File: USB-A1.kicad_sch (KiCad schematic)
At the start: 23 parts, among them J10 USB3_A, J9 USB3_A, U18 UCS2114-1-V/G4, U19 TPD4E02B04DQA, U20 TPD4E02B04DQA, U32 TPD4E02B04DQA

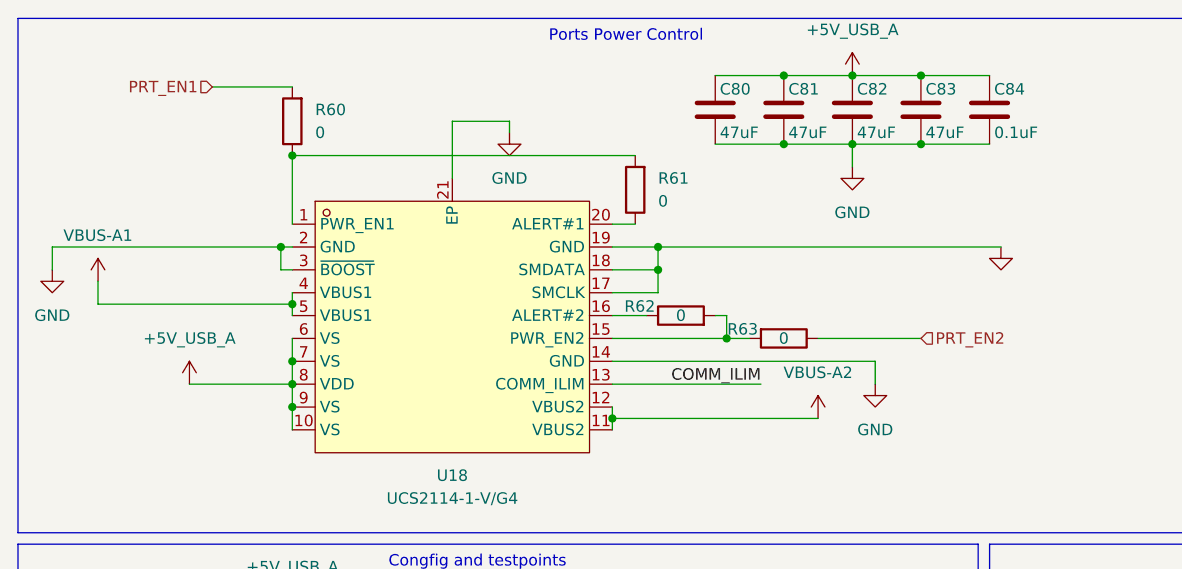
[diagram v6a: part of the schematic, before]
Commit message: minor schematic fixes, footprints changes, layout improvements
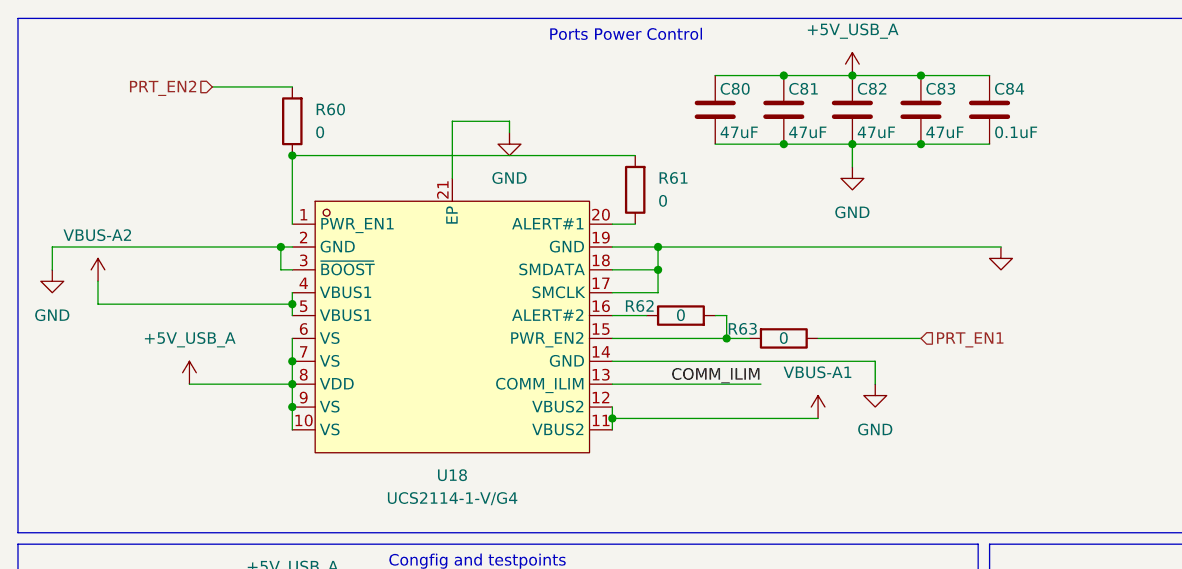
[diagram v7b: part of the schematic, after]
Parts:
- TP5, TP6: footprint TestPoint:TestPoint_Loop_D1.80mm_Drill1.0mm_Beaded -> TestPoint:TestPoint_Pad_D1.0mm
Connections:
- net PRT_EN1: now also R63.1; no longer R60.2
- net PRT_EN2: now also R60.2; no longer R63.1
- net VBUS-A1: now also U18.11 (VBUS2), U18.12 (VBUS2); no longer U18.4 (VBUS1), U18.5 (VBUS1)
- net VBUS-A2: now also U18.4 (VBUS1), U18.5 (VBUS1); no longer U18.11 (VBUS2), U18.12 (VBUS2)
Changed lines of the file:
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@@
 	(hierarchical_label "PRT_EN2"
+		(shape input)
+		(at 36.83 20.32 180)
+		(effects
+			(font
+				(size 1.27 1.27)
+			)
+			(justify right)
+		)
+	)
+	(hierarchical_label "PRT_EN1"
 		(shape input)
 		(at 115.57 48.26 0)
@@
 		)
 	)
-	(hierarchical_label "PRT_EN1"
-		(shape input)
-		(at 36.83 20.32 180)
-		(effects
-			(font
-				(size 1.27 1.27)
-			)
-			(justify right)
-		)
-	)
 	(rule_area
 		(polyline
@@
 	(symbol
 		(lib_id "power:VBUS")
+		(at 104.14 57.15 0)
+		(unit 1)
+		(exclude_from_sim no)
+		(in_bom yes)
+		(on_board yes)
+		(dnp no)
+		(fields_autoplaced yes)
+		(property "Reference" "#PWR0140"
+			(at 104.14 60.96 0)
+			(effects
+				(font
+					(size 1.27 1.27)
+				)
+				(hide yes)
+			)
+		)
+		(property "Value" "VBUS-A1"
+			(at 104.14 52.07 0)
+			(effects
+				(font
+					(size 1.27 1.27)
+				)
+			)
+		)
+		(property "Footprint" ""
+			(at 104.14 57.15 0)
+			(effects
+				(font
+					(size 1.27 1.27)
+				)
+				(hide yes)
+			)
+		)
+		(property "Datasheet" ""
+			(at 104.14 57.15 0)
+			(effects
+				(font
+					(size 1.27 1.27)
+				)
+				(hide yes)
+			)
+		)
+		(property "Description" "Power symbol creates a global label with name \"VBUS\""
+			(at 104.14 57.15 0)
+			(effects
+				(font
+					(size 1.27 1.27)
+				)
+				(hide yes)
+			)
+		)
+		(pin "1"
+		)
+		(instances
+			(project "USB_hub"
+				(path "/a2586c28-95f1-49e6-9254-37d7a8473e53/10c83c9e-05bd-4fa1-b7e1-a721413825c3"
+					(reference "#PWR0140")
+					(unit 1)
+				)
+			)
+		)
+	)
+	(symbol
+		(lib_id "Device:LED")
+		(at 189.23 93.98 180)
+		(unit 1)
+		(exclude_from_sim no)
+		(in_bom yes)
+		(on_board yes)
+		(dnp no)
+		(fields_autoplaced yes)
+		(property "Reference" "D7"
+			(at 190.8175 86.36 0)
+			(effects
+				(font
+					(size 1.27 1.27)
+				)
+			)
+		)
+		(property "Value" "GREEN"
+			(at 190.8175 88.9 0)
+			(effects
+				(font
+					(size 1.27 1.27)
+				)
+			)
+		)
+		(property "Footprint" "LED_SMD:LED_0603_1608Metric"
+			(at 189.23 93.98 0)
+			(effects
+				(font
+					(size 1.27 1.27)
+				)
+				(hide yes)
+			)
+		)
+		(property "Datasheet" "~"
+			(at 189.23 93.98 0)
+			(effects
+				(font
+					(size 1.27 1.27)
+				)
+				(hide yes)
+			)
+		)
+		(property "Description" "Light emitting diode"
+			(at 189.23 93.98 0)
+			(effects
+				(font
+					(size 1.27 1.27)
+				)
+				(hide yes)
+			)
+		)
+		(property "Sim.Pins" "1=K 2=A"
+			(at 189.23 93.98 0)
+			(effects
+				(font
+					(size 1.27 1.27)
+				)
+				(hide yes)
+			)
+		)
+		(property "LCSC Part" "C22371298"
+			(at 189.23 93.98 0)
+			(effects
+				(font
+					(size 1.27 1.27)
+				)
+				(hide yes)
+			)
+		)
+		(pin "1"
+		)
+		(pin "2"
+		)
+		(instances
+			(project "USB_hub"
+				(path "/a2586c28-95f1-49e6-9254-37d7a8473e53/10c83c9e-05bd-4fa1-b7e1-a721413825c3"
+					(reference "D7")
+					(unit 1)
+				)
+			)
+		)
+	)
+	(symbol
+		(lib_id "power:VBUS")
 		(at 24.13 41.91 0)
-		(unit 1)
-		(exclude_from_sim no)
-		(in_bom yes)
-		(on_board yes)
-		(dnp no)
-		(fields_autoplaced yes)
-		(property "Reference" "#PWR0140"
+		(mirror y)
+		(unit 1)
+		(exclude_from_sim no)
+		(in_bom yes)
+		(on_board yes)
+		(dnp no)
+		(fields_autoplaced yes)
+		(property "Reference" "#PWR0143"
 			(at 24.13 45.72 0)
 			(effects
@@
 			)
 		)
-		(property "Value" "VBUS-A1"
+		(property "Value" "VBUS-A2"
 			(at 24.13 36.83 0)
 			(effects
@@
 		(property "Description" "Power symbol creates a global label with name \"VBUS\""
 			(at 24.13 41.91 0)
-			(effects
-				(font
-					(size 1.27 1.27)
-				)
-				(hide yes)
-			)
-		)
-		(pin "1"
-		)
-		(instances
-			(project "USB_hub"
-				(path "/a2586c28-95f1-49e6-9254-37d7a8473e53/10c83c9e-05bd-4fa1-b7e1-a721413825c3"
-					(reference "#PWR0140")
-					(unit 1)
-				)
-			)
-		)
-	)
-	(symbol
-		(lib_id "Device:LED")
-		(at 189.23 93.98 180)
-		(unit 1)
-		(exclude_from_sim no)
-		(in_bom yes)
-		(on_board yes)
-		(dnp no)
-		(fields_autoplaced yes)
-		(property "Reference" "D7"
-			(at 190.8175 86.36 0)
-			(effects
-				(font
-					(size 1.27 1.27)
-				)
-			)
-		)
-		(property "Value" "GREEN"
-			(at 190.8175 88.9 0)
-			(effects
-				(font
-					(size 1.27 1.27)
-				)
-			)
-		)
-		(property "Footprint" "LED_SMD:LED_0603_1608Metric"
-			(at 189.23 93.98 0)
-			(effects
-				(font
-					(size 1.27 1.27)
-				)
-				(hide yes)
-			)
-		)
-		(property "Datasheet" "~"
-			(at 189.23 93.98 0)
-			(effects
-				(font
-					(size 1.27 1.27)
-				)
-				(hide yes)
-			)
-		)
-		(property "Description" "Light emitting diode"
-			(at 189.23 93.98 0)
-			(effects
-				(font
-					(size 1.27 1.27)
-				)
-				(hide yes)
-			)
-		)
-		(property "Sim.Pins" "1=K 2=A"
-			(at 189.23 93.98 0)
-			(effects
-				(font
-					(size 1.27 1.27)
-				)
-				(hide yes)
-			)
-		)
-		(property "LCSC Part" "C22371298"
-			(at 189.23 93.98 0)
-			(effects
-				(font
-					(size 1.27 1.27)
-				)
-				(hide yes)
-			)
-		)
-		(pin "1"
-		)
-		(pin "2"
-		)
-		(instances
-			(project "USB_hub"
-				(path "/a2586c28-95f1-49e6-9254-37d7a8473e53/10c83c9e-05bd-4fa1-b7e1-a721413825c3"
-					(reference "D7")
-					(unit 1)
-				)
-			)
-		)
-	)
-	(symbol
-		(lib_id "power:VBUS")
-		(at 104.14 57.15 0)
-		(mirror y)
-		(unit 1)
-		(exclude_from_sim no)
-		(in_bom yes)
-		(on_board yes)
-		(dnp no)
-		(fields_autoplaced yes)
-		(property "Reference" "#PWR0143"
-			(at 104.14 60.96 0)
-			(effects
-				(font
-					(size 1.27 1.27)
-				)
-				(hide yes)
-			)
-		)
-		(property "Value" "VBUS-A2"
-			(at 104.14 52.07 0)
-			(effects
-				(font
-					(size 1.27 1.27)
-				)
-			)
-		)
-		(property "Footprint" ""
-			(at 104.14 57.15 0)
-			(effects
-				(font
-					(size 1.27 1.27)
-				)
-				(hide yes)
-			)
-		)
-		(property "Datasheet" ""
-			(at 104.14 57.15 0)
-			(effects
-				(font
-					(size 1.27 1.27)
-				)
-				(hide yes)
-			)
-		)
-		(property "Description" "Power symbol creates a global label with name \"VBUS\""
-			(at 104.14 57.15 0)
 			(effects
 				(font
@@
 			)
 		)
-		(property "Footprint" "TestPoint:TestPoint_Loop_D1.80mm_Drill1.0mm_Beaded"
+		(property "Footprint" "TestPoint:TestPoint_Pad_D1.0mm"
 			(at 101.6 82.55 0)
 			(effects
@@
 			)
 		)
-		(property "Footprint" "TestPoint:TestPoint_Loop_D1.80mm_Drill1.0mm_Beaded"
+		(property "Footprint" "TestPoint:TestPoint_Pad_D1.0mm"
 			(at 80.01 82.55 0)
 			(effects

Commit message: comments to schematic added, changed a few components
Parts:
- U18: Mouser Part No  (none) -> 579-UCS2114-1-V/LX
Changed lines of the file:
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@@
+			)
+		)
+		(property "Mouser Part No " "579-UCS2114-1-V/LX "
+			(at 63.5 46.99 0)
+			(effects
+				(font
+					(size 1.27 1.27)
+				)
+				(hide yes)
 			)
 		)
